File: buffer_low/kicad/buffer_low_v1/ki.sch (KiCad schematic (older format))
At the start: 27 parts, among them J1 Header_M1x02, J2 Screw_TermB_01x03, J3 Header_M1x02, J3 J3, U1 TLV4110

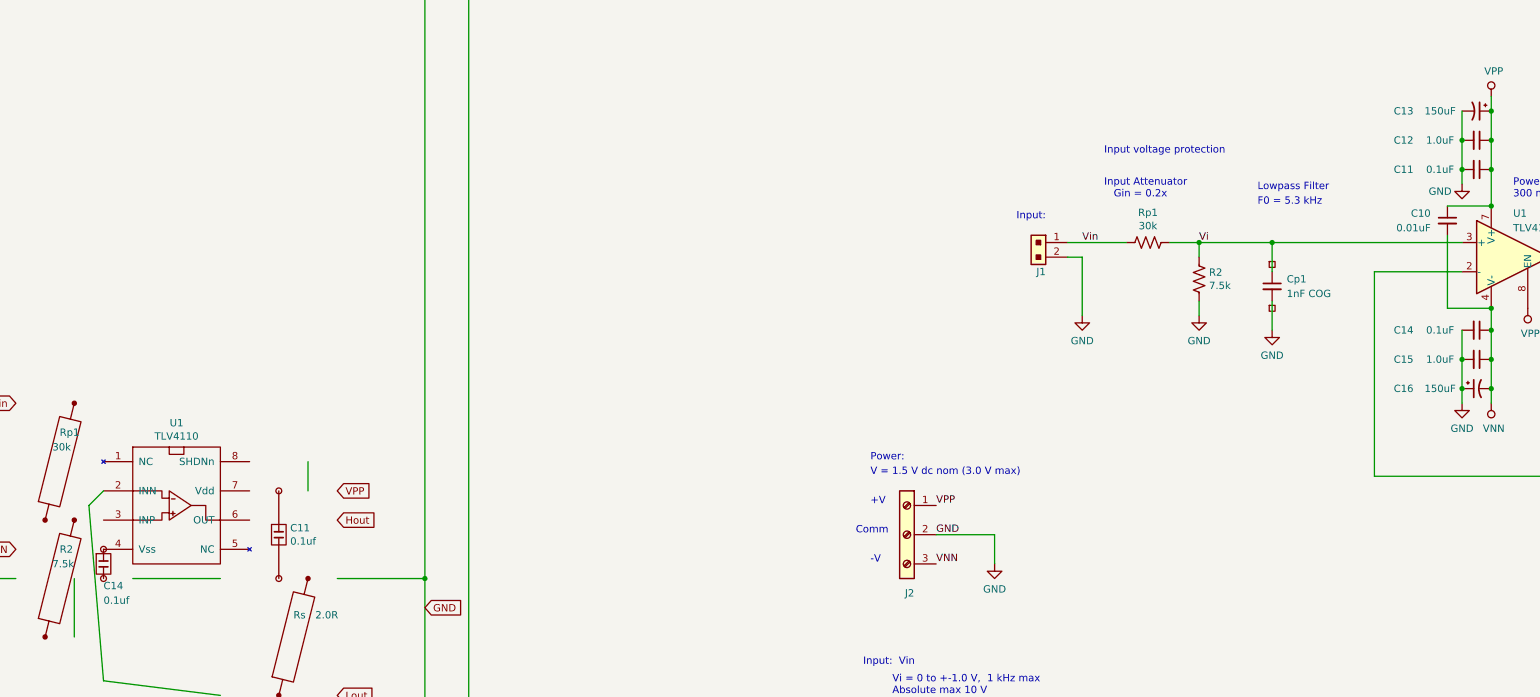
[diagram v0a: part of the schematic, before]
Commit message: buffer_low:  buffer_low_v1/  schematic v1.0.1
    Rename bypass capacitors C2p, C2n, etc. for better association with
    power supply rail.
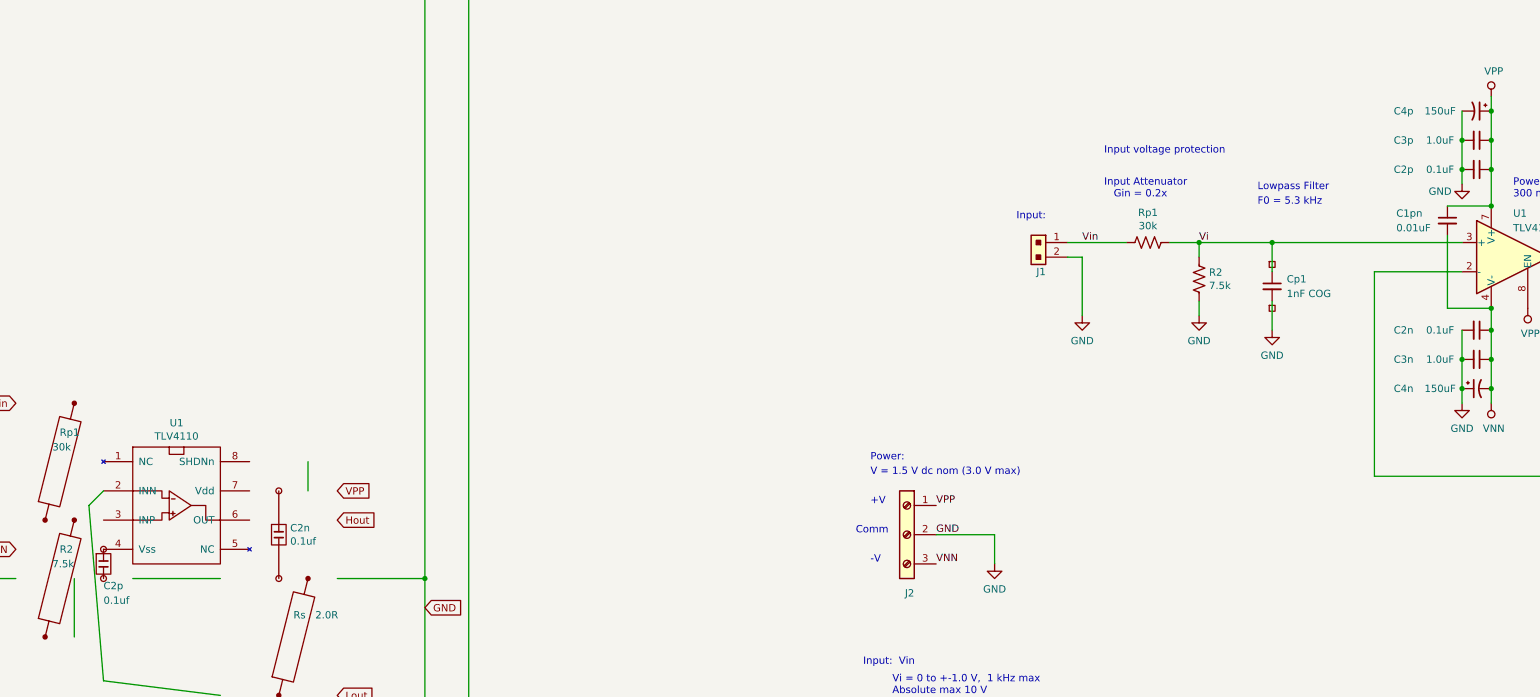
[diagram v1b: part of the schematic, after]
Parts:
- renumbered C10 to C1pn, C14 to C2n, C11 to C2n, C11 to C2p, C14 to C2p, C15 to C3n, C12 to C3p, C16 to C4n, C13 to C4p
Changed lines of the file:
@@
 Sheet 1 1
 Title "Low-Current Buffer - buffer_low_v1/"
-Date "2023-11-11"
-Rev "v1.0.0"
+Date "2023-12-01"
+Rev "v1.0.1"
 Comp "William A. Hudson"
 Comment1 ""
@@
 $EndDescr
 $Comp
-L Device:C_Small C11
+L Device:C_Small C2p
 U 1 1 5EB4CA54
 P 12600 4800
-F 0 "C11" V 12600 4300 50  0000 C CNN
+F 0 "C2p" V 12600 4300 50  0000 C CNN
 F 1 "0.1uF" V 12600 4550 50  0000 C CNN
 F 2 "" H 12600 4800 50  0001 C CNN
@@
 $EndComp
 $Comp
-L Device:C_Small C14
+L Device:C_Small C2n
 U 1 1 5EB4CC2F
 P 12600 5900
-F 0 "C14" V 12600 5400 50  0000 C CNN
+F 0 "C2n" V 12600 5400 50  0000 C CNN
 F 1 "0.1uF" V 12600 5650 50  0000 C CNN
 F 2 "" H 12600 5900 50  0001 C CNN
@@
 $EndComp
 $Comp
-L Device:CP1_Small C13
+L Device:CP1_Small C4p
 U 1 1 5EB4CD7E
 P 12600 4400
-F 0 "C13" V 12600 3900 50  0000 C CNN
+F 0 "C4p" V 12600 3900 50  0000 C CNN
 F 1 "150uF" V 12600 4150 50  0000 C CNN
 F 2 "" H 12600 4400 50  0001 C CNN
@@
 $EndComp
 $Comp
-L Device:CP1_Small C16
+L Device:CP1_Small C4n
 U 1 1 5EB4CEE1
 P 12600 6300
-F 0 "C16" V 12600 6800 50  0000 C CNN
+F 0 "C4n" V 12600 6800 50  0000 C CNN
 F 1 "150uF" V 12600 6550 50  0000 C CNN
 F 2 "" H 12600 6300 50  0001 C CNN
@@
 $EndComp
 $Comp
-L Device:C_Small C10
+L Device:C_Small C1pn
 U 1 1 5EB4D004
 P 12400 5150
-F 0 "C10" H 12150 5200 50  0000 L CNN
+F 0 "C1pn" H 12050 5200 50  0000 L CNN
 F 1 "0.01uF" H 12050 5100 50  0000 L CNN
 F 2 "" H 12400 5150 50  0001 C CNN
@@
 	12700 4400 12700 4600
 $Comp
-L Device:C_Small C12
+L Device:C_Small C3p
 U 1 1 5ED55534
 P 12600 4600
-F 0 "C12" V 12600 4100 50  0000 C CNN
+F 0 "C3p" V 12600 4100 50  0000 C CNN
 F 1 "1.0uF" V 12600 4350 50  0000 C CNN
 F 2 "" H 12600 4600 50  0001 C CNN
@@
 	12500 6300 12500 6100
 $Comp
-L Device:C_Small C15
+L Device:C_Small C3n
 U 1 1 5ED579CE
 P 12600 6100
-F 0 "C15" V 12600 5600 50  0000 C CNN
+F 0 "C3n" V 12600 5600 50  0000 C CNN
 F 1 "1.0uF" V 12600 5850 50  0000 C CNN
 F 2 "" H 12600 6100 50  0001 C CNN
@@
 $EndComp
 $Comp
-L _Breadboard:C1_1_0 C14
+L _Breadboard:C1_1_0 C2p
 U 1 1 6527EEEA
 P 3200 7500
-F 0 "C14" H 3200 7350 50  0000 L CNN
+F 0 "C2p" H 3200 7350 50  0000 L CNN
 F 1 "0.1uf" H 3200 7250 50  0000 L CNN
 F 2 "" H 3200 7500 50  0001 C CNN
@@
 $EndComp
 $Comp
-L _Breadboard:C3_3_0 C11
+L _Breadboard:C3_3_0 C2n
 U 1 1 6527F58E
 P 4400 7300
-F 0 "C11" H 4478 7346 50  0000 L CNN
+F 0 "C2n" H 4478 7346 50  0000 L CNN
 F 1 "0.1uf" H 4478 7255 50  0000 L CNN
 F 2 "" H 4400 7300 50  0001 C CNN

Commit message: buffer_low:  buffer_low_v1/  schematic v1.0.2
    Sense resistor Rs= 2.0 ohm, 1%.  Minor improvements.
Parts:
- Rs: value 2.0R 1/4 W, 5% -> 2.0R 1/4 W, 1%
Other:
- note added: "Gin = 1 / ((Rp1 / R2) + 1) Input gain <1.0"
- note added: "Resistors: 1/4 W, 5% Carbon (1% for accuracy)"
- note added: "Rload = 8 ohm, Exciter"
- note removed: "8 ohm, Exciter"
- note removed: "Gin = 1 / (Rp1 / R2) + 1) Input gain <1.0"
- note removed: "Resistors: 1/4 W, 5% Carbon"
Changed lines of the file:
@@
 Sheet 1 1
 Title "Low-Current Buffer - buffer_low_v1/"
-Date "2023-12-01"
-Rev "v1.0.1"
+Date "2023-12-23"
+Rev "v1.0.2"
 Comp "William A. Hudson"
-Comment1 ""
-Comment2 ""
+Comment1 "v1.0.1  Rename bypass capacitors"
+Comment2 "v1.0.2  Rs= 2.0 ohm, 1%"
 Comment3 ""
 Comment4 ""
@@
 P 13400 7150
 F 0 "Rs" H 13332 7104 50  0000 R CNN
-F 1 "2.0R  1/4 W, 5%" H 13332 7195 50  0000 R CNN
+F 1 "2.0R  1/4 W, 1%" H 13332 7195 50  0000 R CNN
 F 2 "" V 13440 7140 50  0001 C CNN
 F 3 "~" H 13400 7150 50  0001 C CNN
@@
 Current Buffer:  0.1 mA/mV, 100 mA Full Scale
 Text Notes 8400 10000 0    50   ~ 0
-Resistors:  1/4 W, 5% Carbon
+Resistors:  1/4 W, 5% Carbon (1% for accuracy)
 $Comp
 L Device:D_Schottky_Small_ALT D2
@@
 	14750 5600 14850 5600
 Text Notes 15000 5600 0    50   ~ 0
-8 ohm, Exciter
+Rload = 8 ohm, Exciter
 Wire Wire Line
 	13800 5500 13400 5500
@@
 Input Attenuator:
 Text Notes 8600 9500 0    50   ~ 0
-Gin = 1 / (Rp1 / R2) + 1)       Input gain <1.0
+Gin = 1 / ((Rp1 / R2) + 1)       Input gain <1.0
 Text Notes 8600 9600 0    50   ~ 0
 Rp1 / R2 = (1 / Gin) - 1
